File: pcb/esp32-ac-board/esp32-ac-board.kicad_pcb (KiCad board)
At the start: 2 copper layers, 82.8 x 52.6 mm, 12 parts, among them J1 Conn_01x15, J2 Conn_01x15, Q1 Q_NPN_BCE, SW1 SW_Push

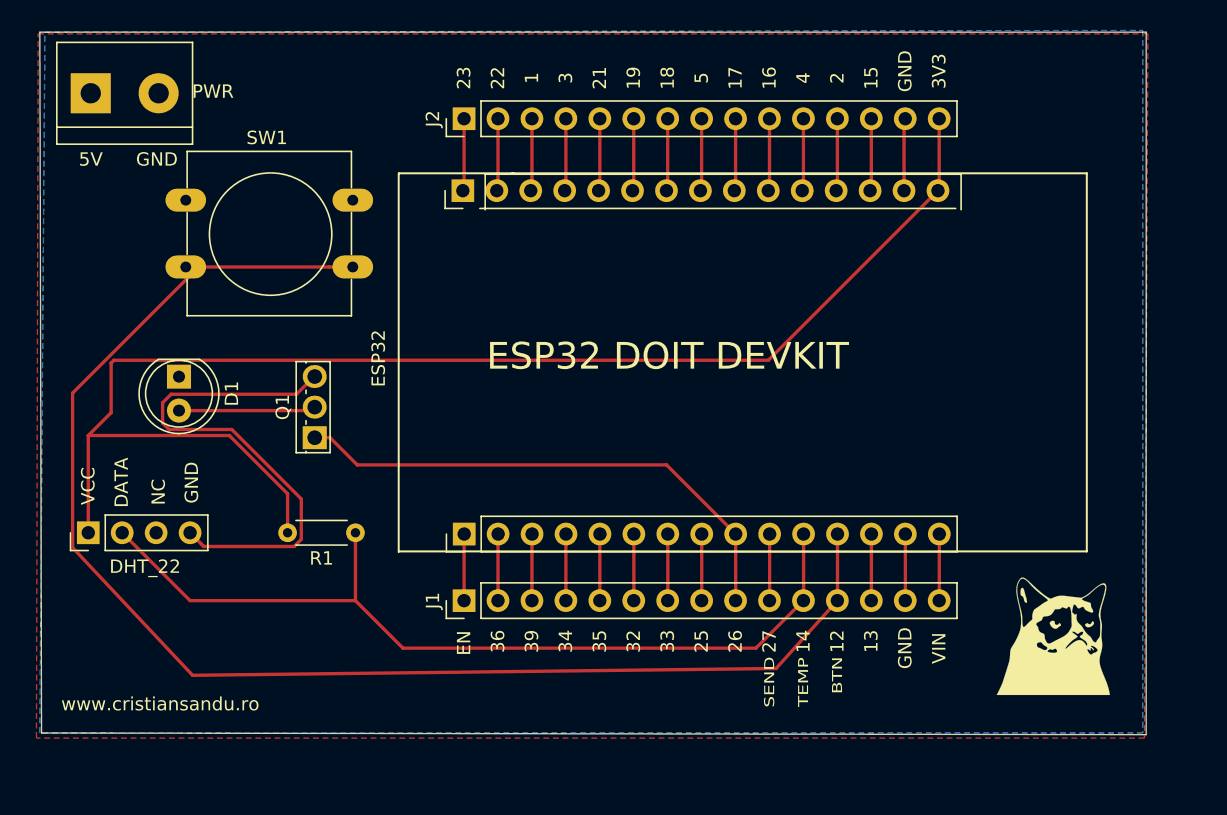
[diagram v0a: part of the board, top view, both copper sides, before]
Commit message: v0.1 sent to JLCPCB.com
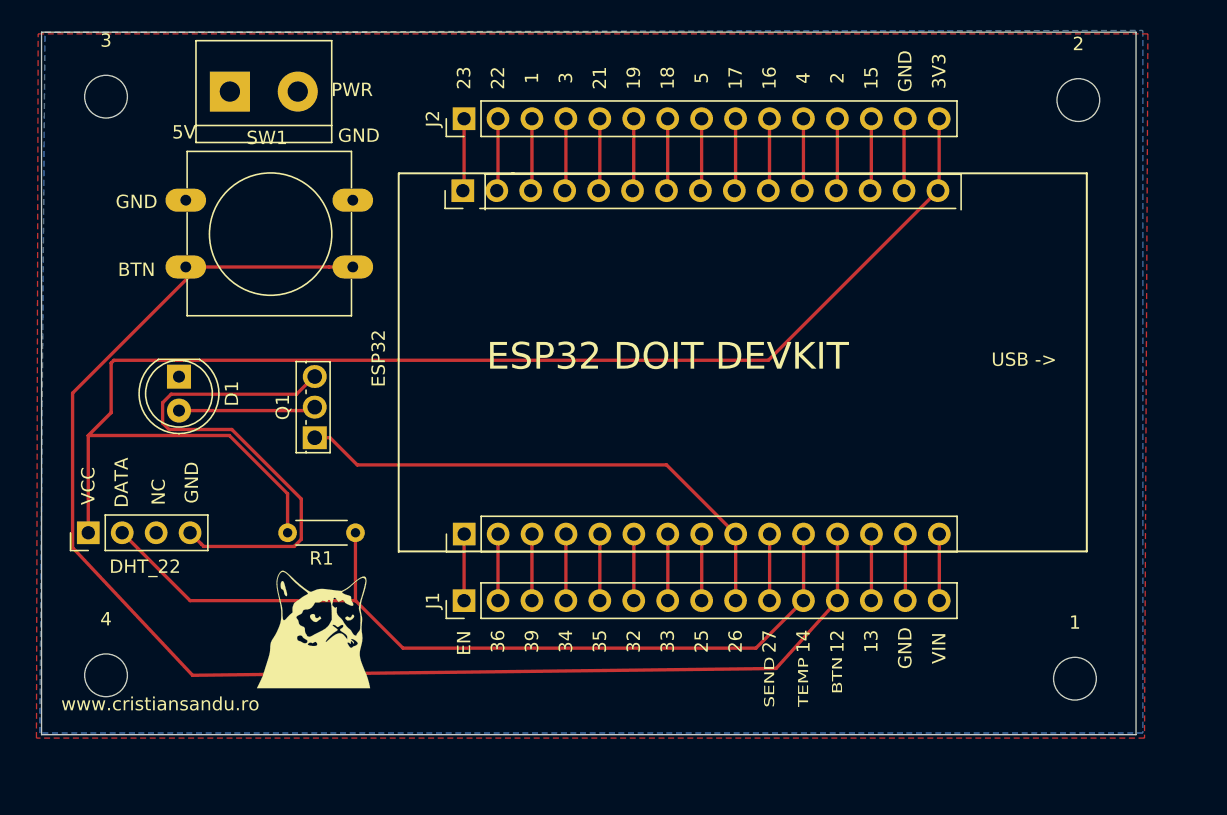
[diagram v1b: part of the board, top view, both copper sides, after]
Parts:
- added 1: MountingHole_3.2mm_M3, MountingHole:MountingHole_3.2mm_M3, F.Cu at (199.1, 115.6)
- added 2: MountingHole_3.2mm_M3, MountingHole:MountingHole_3.2mm_M3, F.Cu at (199.4, 72.3)
- added 3: MountingHole_3.2mm_M3, MountingHole:MountingHole_3.2mm_M3, F.Cu at (126.6, 72.0)
- added 4: MountingHole_3.2mm_M3, MountingHole:MountingHole_3.2mm_M3, F.Cu at (126.6, 115.3)
- moved G*** 55.4 mm to (142.1, 111.5)
- moved PWR 10.4 mm to (135.9, 71.6)
- moved LOGO 1.49 mm to (137.0, 110.0)
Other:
- board size 82.8 x 52.6 mm -> 81.9 x 52.6 mm
- board text added: "1"
- board text added: "11"
- board text added: "12"
- board text added: "13"
- board text added: "15"
- board text added: "16"
- board text added: "17"
- board text added: "18"
- board text added: "19"
- board text added: "2"
- board text added: "21"
- board text added: "22"
- board text added: "23"
- board text added: "25"
- board text added: "27"
- board text added: "3"
- board text added: "32"
- board text added: "33"
- board text added: "34"
- board text added: "35"
- board text added: "36"
- board text added: "39"
- board text added: "3V3"
- board text added: "4"
- board text added: "5"
- board text added: "9"
- board text added: "EN"
- board text added: "USB ->"

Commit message: attempt to rotate diode
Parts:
- renumbered PWR to J3
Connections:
- D1 pad 1: +5V -> Net-(D1-Pad1)
- D1 pad 2: Net-(D1-Pad2) -> +5V
- Q1 pad 2: Net-(D1-Pad2) -> Net-(D1-Pad1)
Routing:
- net GND: track 48.9 -> 10.5 mm
- net Net-(D1-Pad1): track 0.00 -> 11.5 mm
- net /BTN: track 106.0 -> 95.3 mm
- net Net-(D1-Pad2): track 10.3 -> 0.00 mm
